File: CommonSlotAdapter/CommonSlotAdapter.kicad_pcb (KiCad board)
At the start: 2 copper layers, 109.2 x 35.6 mm, 16 parts, among them J1 Val**, J2 XT90, J3 XT60, J4 XT60, J5 RedCube_P, J6 RedCube_N, J7 Banana_P, J8 Banana_N, SW1 ON/OFF

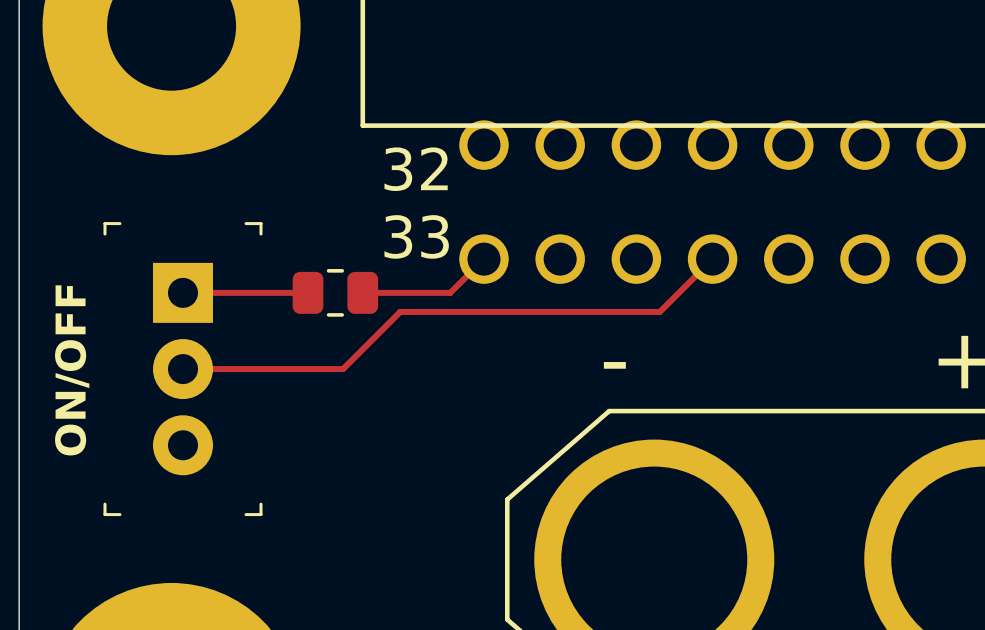
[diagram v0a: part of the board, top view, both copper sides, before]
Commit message: Issue with power output enable
Version 1 didn't work, version 2 is working
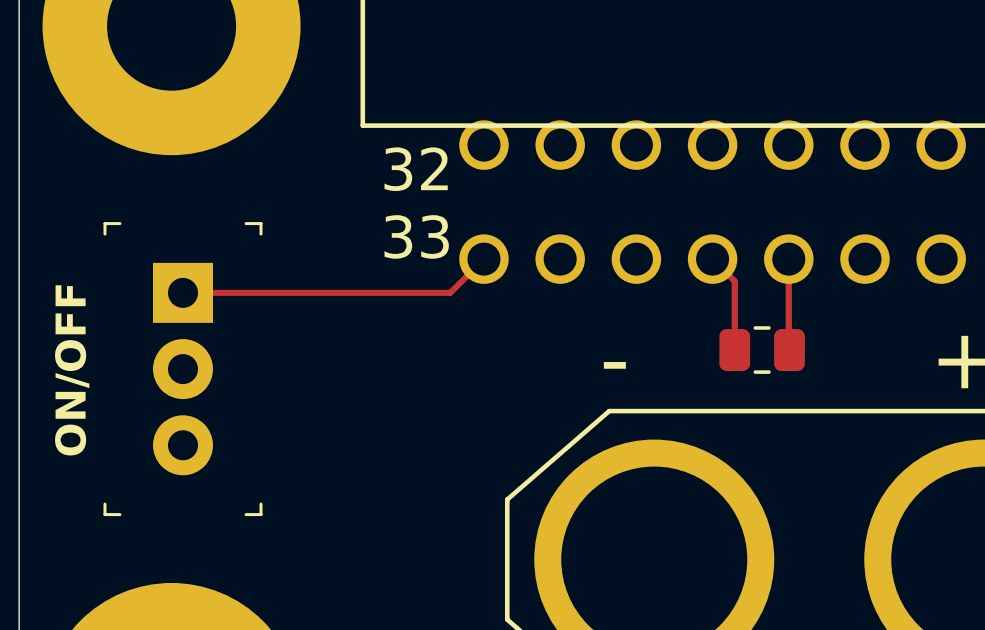
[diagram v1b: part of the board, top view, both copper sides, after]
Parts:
- J1: value Val** -> 10053363-200LF
- R1: value 1K -> 22K
- moved R1 14.4 mm to (108.6, 79.4)
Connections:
- J1 pad 37: unconnected-(J1-Pin_37-Pad37) -> Net-(J1-Pin_37)
- R1 pad 1: Net-(SW1-B) -> Net-(J1-Pin_36)
- R1 pad 2: Net-(J1-Pin_33) -> Net-(J1-Pin_37)
- SW1 pad 1: Net-(SW1-B) -> Net-(J1-Pin_33)
- SW1 pad 2: Net-(J1-Pin_36) -> GND
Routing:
- net Net-(J1-Pin_36): track 19.2 -> 3.34 mm
- net Net-(J1-Pin_33): track 4.51 -> 10.5 mm
- net Net-(SW1-B): track 4.17 -> 0.00 mm
- net Net-(J1-Pin_37): track 0.00 -> 3.04 mm
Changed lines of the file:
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@@
 	(net 4 "+12V")
 	(net 5 "unconnected-(J1-Pin_27-Pad27)")
-	(net 6 "unconnected-(J1-Pin_37-Pad37)")
+	(net 6 "Net-(J1-Pin_37)")
 	(net 7 "unconnected-(J1-Pin_29-Pad29)")
 	(net 8 "unconnected-(J1-Pin_32-Pad32)")
@@
 	(net 14 "unconnected-(J1-Pin_28-Pad28)")
 	(net 15 "unconnected-(J1-Pin_31-Pad31)")
-	(net 16 "Net-(SW1-B)")
-	(net 17 "unconnected-(SW1-A-Pad3)")
+	(net 16 "unconnected-(SW1-A-Pad3)")
 	(footprint "Common_slot2:10053363-200LF"
 		(layer "F.Cu")
@@
 			)
 		)
-		(property "Value" "Val**"
+		(property "Value" "10053363-200LF"
 			(at 0 0 0)
 			(layer "F.Fab")
@@
 			(net 5 "unconnected-(J1-Pin_27-Pad27)")
 			(pinfunction "Pin_27")
-			(pintype "passive")
+			(pintype "passive+no_connect")
 			(solder_mask_margin 0.1016)
 			(thermal_bridge_angle 0)
@@
 			(net 14 "unconnected-(J1-Pin_28-Pad28)")
 			(pinfunction "Pin_28")
-			(pintype "passive")
+			(pintype "passive+no_connect")
 			(solder_mask_margin 0.1016)
 			(thermal_bridge_angle 0)
@@
 			(net 7 "unconnected-(J1-Pin_29-Pad29)")
 			(pinfunction "Pin_29")
-			(pintype "passive")
+			(pintype "passive+no_connect")
 			(solder_mask_margin 0.1016)
 			(thermal_bridge_angle 0)
@@
 			(net 10 "unconnected-(J1-Pin_30-Pad30)")
 			(pinfunction "Pin_30")
-			(pintype "passive")
+			(pintype "passive+no_connect")
 			(solder_mask_margin 0.1016)
 			(thermal_bridge_angle 0)
@@
 			(net 15 "unconnected-(J1-Pin_31-Pad31)")
 			(pinfunction "Pin_31")
-			(pintype "passive")
+			(pintype "passive+no_connect")
 			(solder_mask_margin 0.1016)
 			(thermal_bridge_angle 0)
@@
 			(net 8 "unconnected-(J1-Pin_32-Pad32)")
 			(pinfunction "Pin_32")
-			(pintype "passive")
+			(pintype "passive+no_connect")
 			(solder_mask_margin 0.1016)
 			(thermal_bridge_angle 0)
@@
 			(layers "*.Cu" "*.Mask")
 			(remove_unused_layers no)
-			(net 6 "unconnected-(J1-Pin_37-Pad37)")
+			(net 6 "Net-(J1-Pin_37)")
 			(pinfunction "Pin_37")
 			(pintype "passive")
@@
 	(footprint "Resistor_SMD:R_0805_2012Metric"
 		(layer "F.Cu")
-		(at 94.361 77.47)
+		(at 108.585 79.375)
 		(descr "Resistor SMD 0805 (2012 Metric), square (rectangular) end terminal, IPC_7351 nominal, (Body size source: IPC-SM-782 page 72, https://www.pcb-3d.com/wordpress/wp-content/uploads/ipc-sm-782a_amendment_1_and_2.pdf), generated with kicad-footprint-generator")
 		(tags "resistor")
@@
 			)
 		)
-		(property "Value" "1K"
+		(property "Value" "22K"
 			(at 0 1.65 0)
 			(layer "F.Fab")
@@
 			(layers "F.Cu" "F.Paste" "F.Mask")
 			(roundrect_rratio 0.243902)
-			(net 16 "Net-(SW1-B)")
+			(net 9 "Net-(J1-Pin_36)")
 			(pintype "passive")
 		)
@@
 			(layers "F.Cu" "F.Paste" "F.Mask")
 			(roundrect_rratio 0.243902)
-			(net 12 "Net-(J1-Pin_33)")
+			(net 6 "Net-(J1-Pin_37)")
 			(pintype "passive")
 		)
@@
 			(layers "*.Cu" "*.Mask")
 			(remove_unused_layers no)
-			(net 16 "Net-(SW1-B)")
+			(net 12 "Net-(J1-Pin_33)")
 			(pinfunction "B")
 			(pintype "passive")
@@
 			(layers "*.Cu" "*.Mask")
 			(remove_unused_layers no)
-			(net 9 "Net-(J1-Pin_36)")
+			(net 1 "GND")
 			(pinfunction "C")
 			(pintype "passive")
@@
 			(layers "*.Cu" "*.Mask")
 			(remove_unused_layers no)
-			(net 17 "unconnected-(SW1-A-Pad3)")
+			(net 16 "unconnected-(SW1-A-Pad3)")
 			(pinfunction "A")
-			(pintype "passive")
+			(pintype "passive+no_connect")
 		)
 		(model "${CGRANTKICADLIBRARIES}/Switches/ATE1D-2M3-10-Z.STEP"
@@
 	)
 	(segment
-		(start 96.52 78.105)
-		(end 105.1736 78.105)
+		(start 109.474 76.3446)
+		(end 109.474 79.3515)
 		(width 0.2)
 		(layer "F.Cu")
-		(net 9)
+		(net 6)
 	)
 	(segment
-		(start 105.1736 78.105)
-		(end 106.934 76.3446)
+		(start 109.474 79.3515)
+		(end 109.4975 79.375)
 		(width 0.2)
 		(layer "F.Cu")
-		(net 9)
+		(net 6)
 	)
 	(segment
-		(start 94.615 80.01)
-		(end 96.52 78.105)
+		(start 107.6725 79.375)
+		(end 107.6725 77.0831)
 		(width 0.2)
 		(layer "F.Cu")
@@
 	)
 	(segment
-		(start 89.281 80.01)
-		(end 94.615 80.01)
+		(start 107.6725 77.0831)
+		(end 106.934 76.3446)
 		(width 0.2)
 		(layer "F.Cu")
@@
 	)
 	(segment
-		(start 95.2735 77.47)
+		(start 89.281 77.47)
 		(end 98.1886 77.47)
 		(width 0.2)
@@
 		(net 12)
 	)
-	(segment
-		(start 89.281 77.47)
-		(end 93.4485 77.47)
-		(width 0.2)
-		(layer "F.Cu")
-		(net 16)
-	)
 	(zone
